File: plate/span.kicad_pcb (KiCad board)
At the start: 2 copper layers, 111.6 x 95.2 mm, 23 parts, among them SW19 SW_PUSH, SW20 SW_PUSH, SW21 SW_PUSH, SW22 SW_PUSH, SW23 SW_PUSH, SW24 SW_PUSH, SW25 SW_PUSH, SW26 SW_PUSH, SW27 SW_PUSH, SW28 SW_PUSH, SW29 SW_PUSH, SW30 SW_PUSH, SW31 SW_PUSH, SW32 SW_PUSH, SW33 SW_PUSH, SW34 SW_PUSH, SW35 SW_PUSH, SW36 SW_PUSH

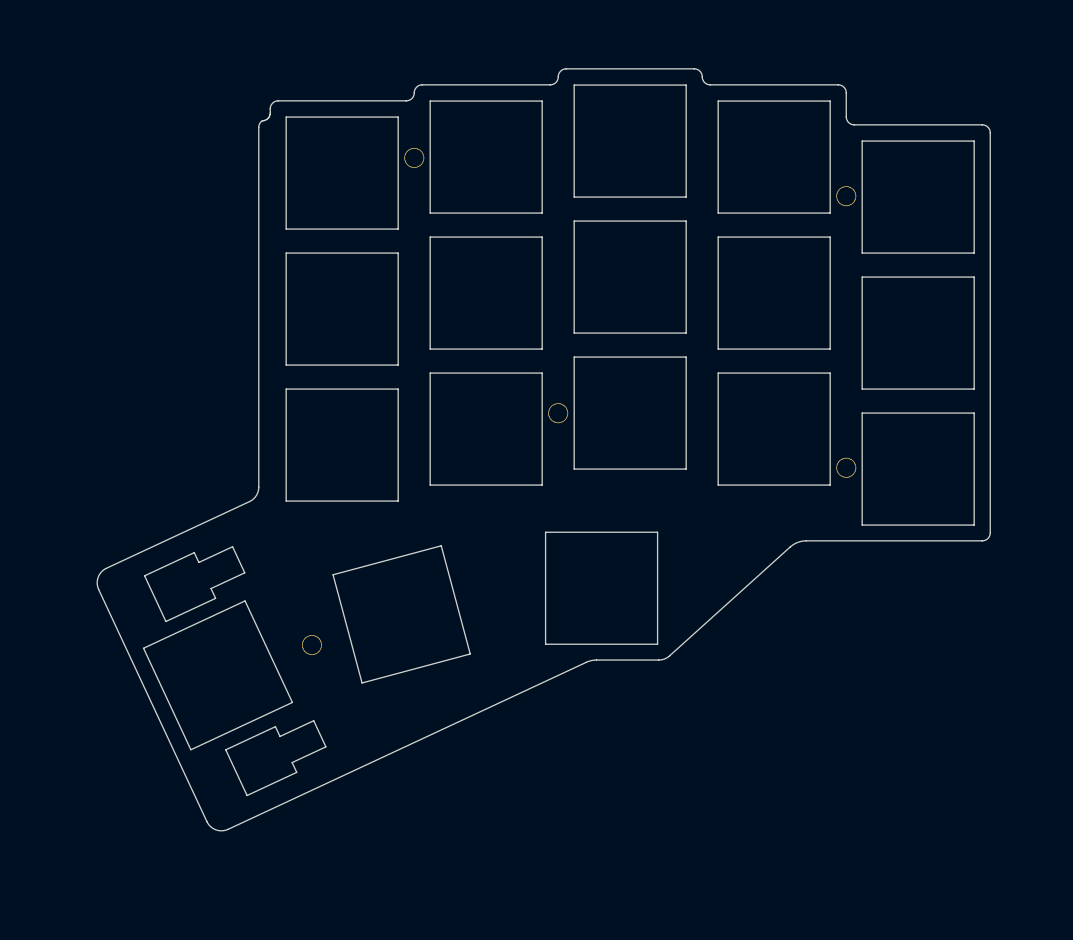
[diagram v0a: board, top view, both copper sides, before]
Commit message: pcb: add filled zones
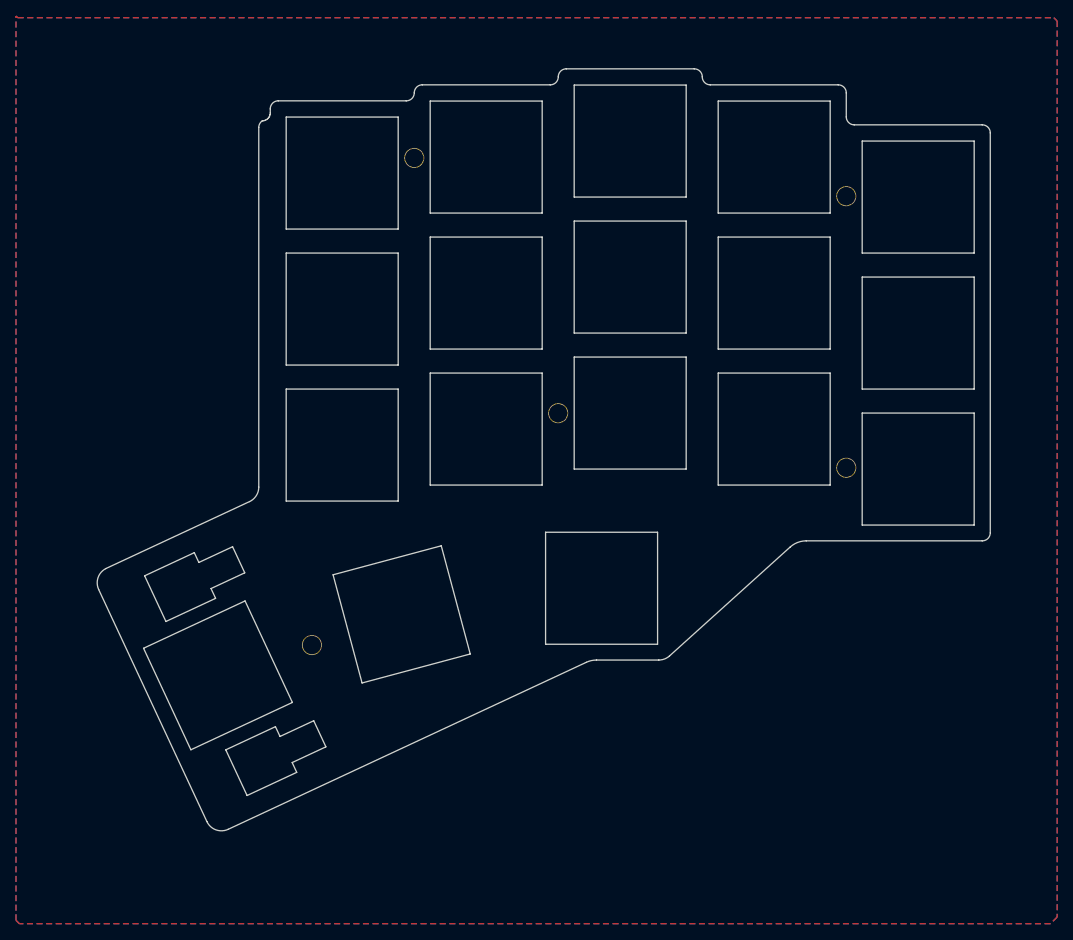
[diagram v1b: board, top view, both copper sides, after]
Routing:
- added copper zone on B.Cu, net (none)
- added copper zone on F.Cu, net (none)
